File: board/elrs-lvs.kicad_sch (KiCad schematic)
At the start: 150 parts, among them J1 PWM, J10 CF/Prog, J11 Holes, J12 Balance, J13 U.FL, J2 PWM, J3 PWM, J4 PWM, J5 PWM, J6 PWM, J7 PWM, J8 PWM, J9 Little Tower, SW1 SW_SPST, SW2 SW_SPST, U1 ESP32-PICO-V3, U2 SX1281, U3 TPSM82901SISR, U4 2450FM07D0034T, Y1 52Mhz TCXO

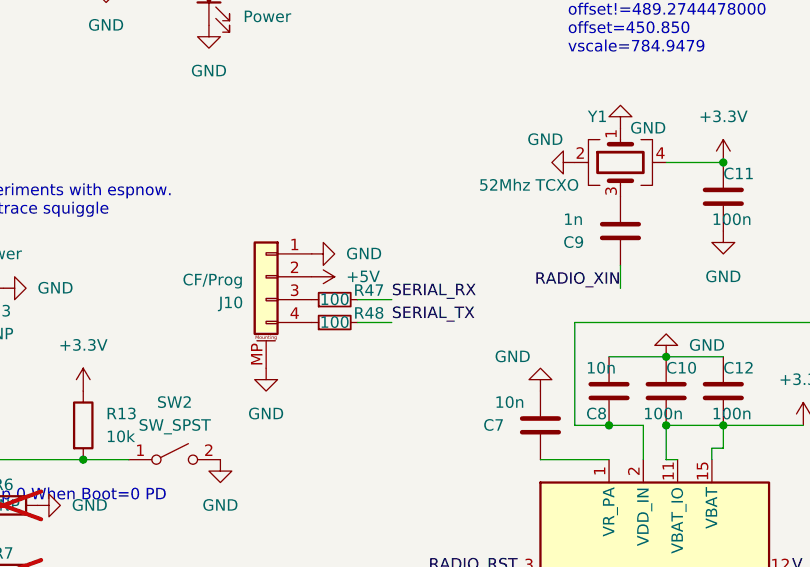
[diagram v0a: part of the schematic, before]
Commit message: invert serial connector pinout
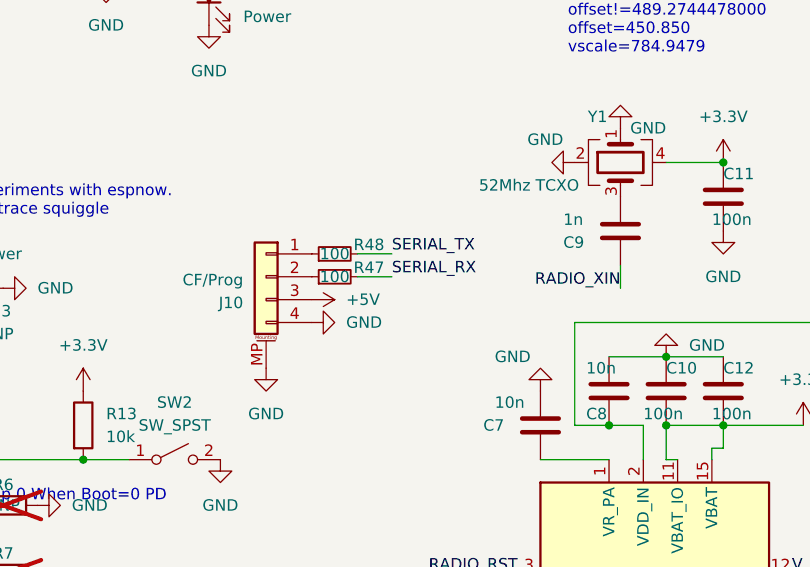
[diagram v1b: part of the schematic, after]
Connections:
- net +5V: now also J10.3 (Pin_3); no longer J10.2 (Pin_2)
- net GND: now also J10.4 (Pin_4); no longer J10.1 (Pin_1)
- net at R48.1: now also J10.1 (Pin_1); no longer J10.4 (Pin_4)
- net at R47.1: now also J10.2 (Pin_2); no longer J10.3 (Pin_3)
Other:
- moved on the sheet: R47, R48
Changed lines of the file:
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@@
 	(wire
 		(pts
-			(xy 157.48 72.39) (xy 161.29 72.39)
+			(xy 157.48 64.77) (xy 161.29 64.77)
 		)
 		(stroke
@@
 	(wire
 		(pts
-			(xy 157.48 69.85) (xy 161.29 69.85)
+			(xy 157.48 67.31) (xy 161.29 67.31)
 		)
 		(stroke
@@
 	)
 	(label "SERIAL_TX"
-		(at 161.29 72.39 0)
+		(at 161.29 64.77 0)
 		(effects
 			(font
@@
 	)
 	(label "SERIAL_RX"
-		(at 161.29 69.85 0)
+		(at 161.29 67.31 0)
 		(effects
 			(font
@@
 	(symbol
 		(lib_id "Device:R_Small")
-		(at 154.94 72.39 90)
+		(at 154.94 64.77 90)
 		(unit 1)
 		(exclude_from_sim no)
@@
 		(dnp no)
 		(property "Reference" "R48"
-			(at 158.75 71.374 90)
+			(at 158.75 63.754 90)
 			(effects
 				(font
@@
 		)
 		(property "Value" "100"
-			(at 154.94 72.39 90)
+			(at 154.94 64.77 90)
 			(effects
 				(font
@@
 		)
 		(property "Footprint" "Resistor_SMD:R_0402_1005Metric"
-			(at 154.94 72.39 0)
+			(at 154.94 64.77 0)
 			(effects
 				(font
@@
 		)
 		(property "Datasheet" "~"
-			(at 154.94 72.39 0)
+			(at 154.94 64.77 0)
 			(effects
 				(font
@@
 		)
 		(property "Description" "Resistor, small symbol"
-			(at 154.94 72.39 0)
+			(at 154.94 64.77 0)
 			(effects
 				(font
@@
 		)
 		(property "Digikey" "https://www.digikey.com/en/products/detail/yageo/AC0402JR-07100RL/5895570"
-			(at 154.94 72.39 0)
+			(at 154.94 64.77 0)
 			(effects
 				(font
@@
 		)
 		(property "Manufacturer" "Yageo"
-			(at 154.94 72.39 0)
+			(at 154.94 64.77 0)
 			(effects
 				(font
@@
 		)
 		(property "Part" "AC0402JR-07100RL"
-			(at 154.94 72.39 0)
+			(at 154.94 64.77 0)
 			(effects
 				(font
@@
 	(symbol
 		(lib_id "Device:R_Small")
-		(at 154.94 69.85 90)
+		(at 154.94 67.31 90)
 		(unit 1)
 		(exclude_from_sim no)
@@
 		(dnp no)
 		(property "Reference" "R47"
-			(at 158.75 68.834 90)
+			(at 158.75 66.294 90)
 			(effects
 				(font
@@
 		)
 		(property "Value" "100"
-			(at 154.94 69.85 90)
+			(at 154.94 67.31 90)
 			(effects
 				(font
@@
 		)
 		(property "Footprint" "Resistor_SMD:R_0402_1005Metric"
-			(at 154.94 69.85 0)
+			(at 154.94 67.31 0)
 			(effects
 				(font
@@
 		)
 		(property "Datasheet" "~"
-			(at 154.94 69.85 0)
+			(at 154.94 67.31 0)
 			(effects
 				(font
@@
 		)
 		(property "Description" "Resistor, small symbol"
-			(at 154.94 69.85 0)
+			(at 154.94 67.31 0)
 			(effects
 				(font
@@
 		)
 		(property "Digikey" "https://www.digikey.com/en/products/detail/yageo/AC0402JR-07100RL/5895570"
-			(at 154.94 69.85 0)
+			(at 154.94 67.31 0)
 			(effects
 				(font
@@
 		)
 		(property "Manufacturer" "Yageo"
-			(at 154.94 69.85 0)
+			(at 154.94 67.31 0)
 			(effects
 				(font
@@
 		)
 		(property "Part" "AC0402JR-07100RL"
-			(at 154.94 69.85 0)
+			(at 154.94 67.31 0)
 			(effects
 				(font
@@
 	(symbol
 		(lib_id "power:+5V")
-		(at 152.4 67.31 270)
+		(at 152.4 69.85 270)
 		(unit 1)
 		(exclude_from_sim no)
@@
 		(fields_autoplaced yes)
 		(property "Reference" "#PWR051"
-			(at 148.59 67.31 0)
+			(at 148.59 69.85 0)
 			(effects
 				(font
@@
 		)
 		(property "Value" "+5V"
-			(at 156.21 67.3099 90)
+			(at 156.21 69.8499 90)
 			(effects
 				(font
@@
 		)
 		(property "Footprint" ""
-			(at 152.4 67.31 0)
+			(at 152.4 69.85 0)
 			(effects
 				(font
@@
 		)
 		(property "Datasheet" ""
-			(at 152.4 67.31 0)
+			(at 152.4 69.85 0)
 			(effects
 				(font
@@
 		)
 		(property "Description" "Power symbol creates a global label with name \"+5V\""
-			(at 152.4 67.31 0)
+			(at 152.4 69.85 0)
 			(effects
 				(font
@@
 	(symbol
 		(lib_id "power:GND")
-		(at 152.4 64.77 90)
+		(at 152.4 72.39 90)
 		(unit 1)
 		(exclude_from_sim no)
@@
 		(fields_autoplaced yes)
 		(property "Reference" "#PWR050"
-			(at 158.75 64.77 0)
+			(at 158.75 72.39 0)
 			(effects
 				(font
@@
 		)
 		(property "Value" "GND"
-			(at 156.21 64.7699 90)
+			(at 156.21 72.3899 90)
 			(effects
 				(font
@@
 		)
 		(property "Footprint" ""
-			(at 152.4 64.77 0)
+			(at 152.4 72.39 0)
 			(effects
 				(font
@@
 		)
 		(property "Datasheet" ""
-			(at 152.4 64.77 0)
+			(at 152.4 72.39 0)
 			(effects
 				(font
@@
 		)
 		(property "Description" "Power symbol creates a global label with name \"GND\" , ground"
-			(at 152.4 64.77 0)
+			(at 152.4 72.39 0)
 			(effects
 				(font

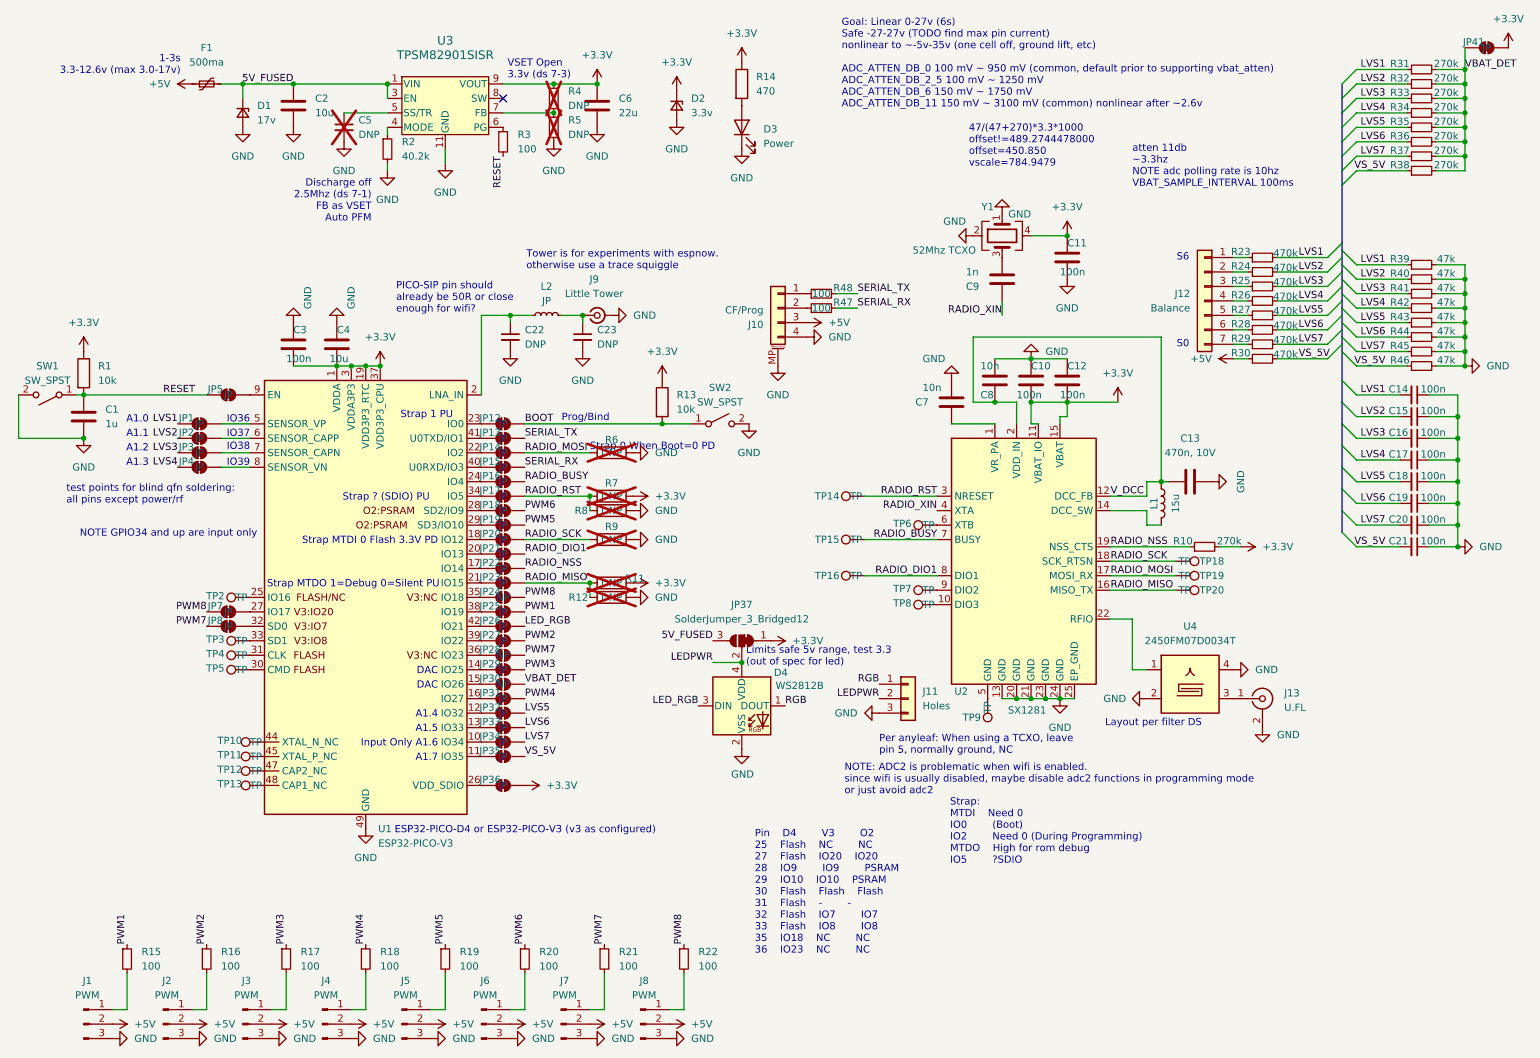
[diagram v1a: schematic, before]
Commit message: remove dnp options and test points
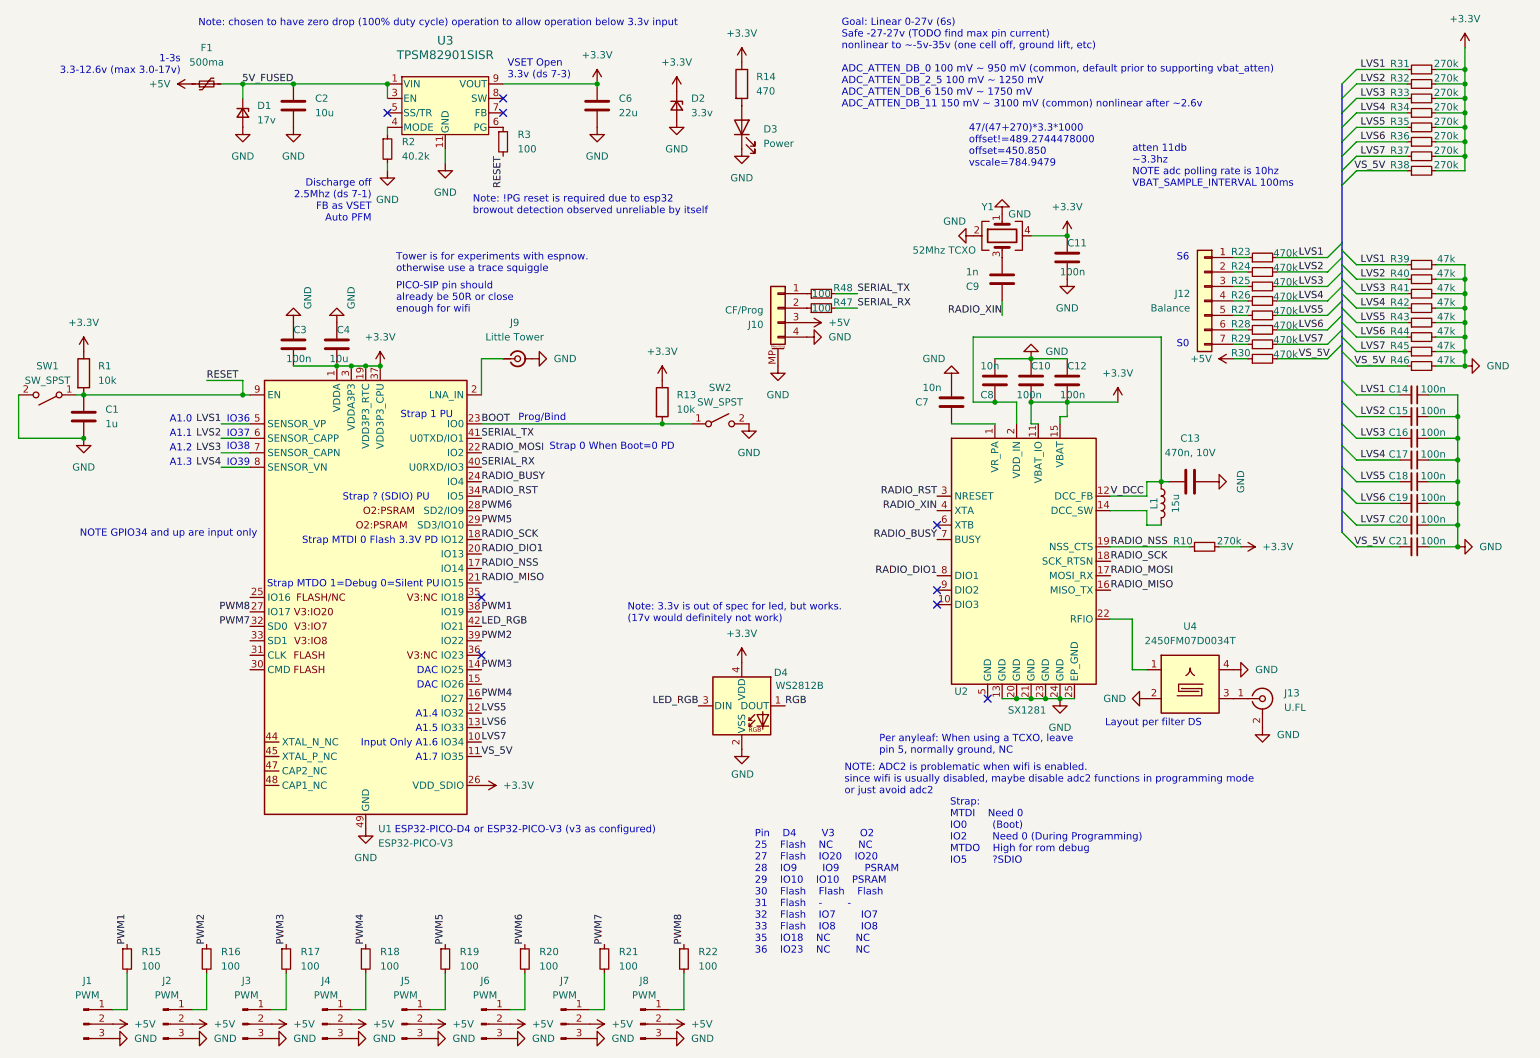
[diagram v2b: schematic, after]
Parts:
- removed C22, C23: DNP, elrs-lvs:R_0201_0603_NP, symbol Device:C_Small
- removed C5: DNP, Capacitor_SMD:C_0402_1005Metric, symbol Device:C_Small
- removed J11: Holes, Connector_PinHeader_2.54mm:PinHeader_1x03_P2.54mm_Vertical, symbol Connector_Generic:Conn_01x03
- removed JP1, JP12, JP13, JP14, JP15, JP16, JP17, JP18, JP19, JP2, JP20, JP21, JP22, JP23, JP25, JP26, JP27, JP29, JP3, JP31, JP32, JP33, JP34, JP35, JP36, JP4, JP41, JP5, JP7, JP8: JP, elrs-lvs:R_0201_0603_JP, symbol Jumper:SolderJumper_2_Bridged
- removed JP24, JP28, JP30: NP, elrs-lvs:R_0201_0603_NP, symbol Jumper:SolderJumper_2_Open
- removed JP37: SolderJumper_3_Bridged12, elrs-lvs:R_0201_0603_JP_123, symbol Jumper:SolderJumper_3_Bridged12
- removed L2: JP, elrs-lvs:R_0201_0603_JP, symbol Device:L_Small
- removed R11, R12, R6, R7, R8, R9: DNP, Resistor_SMD:R_0402_1005Metric, symbol Device:R
- removed R4, R5: DNP, Resistor_SMD:R_0402_1005Metric, symbol Device:R_Small
- removed TP10, TP11, TP12, TP13, TP14, TP15, TP16, TP18, TP19, TP2, TP20, TP3, TP4, TP5, TP6, TP7, TP8, TP9: TP, elrs-lvs:TestPoint_Pad_D0.25mm, symbol Connector:TestPoint
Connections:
- net LEDPWR is gone; now on net +3.3V: D4.4 (VDD)
- net VBAT_DET is gone; now on net +3.3V: R31.2, R32.2, R33.2, R34.2, R35.2, R36.2, R37.2, R38.2
- net +3.3V: now also U1.26 (VDD_SDIO)
- net BOOT: now also U1.23 (IO0)
- net LED_RGB: now also U1.42 (IO21)
- net LVS1: now also U1.5 (SENSOR_VP)
- net LVS2: now also U1.6 (SENSOR_CAPP)
- net LVS3: now also U1.7 (SENSOR_CAPN)
- net LVS4: now also U1.8 (SENSOR_VN)
- net LVS5: now also U1.12 (IO32)
- net LVS6: now also U1.13 (IO33)
- net LVS7: now also U1.10 (IO34)
- net PWM1: now also U1.38 (IO19)
- net PWM2: now also U1.39 (IO22)
- net PWM3: now also U1.14 (IO25)
- net PWM4: now also U1.16 (IO27)
- net PWM5: now also U1.29 (SD3/IO10)
- net PWM6: now also U1.28 (SD2/IO9)
- net PWM7: now also U1.32 (SD0)
- net PWM8: now also U1.27 (IO17)
- net RADIO_BUSY: now also U1.24 (IO4)
- net RADIO_DIO1: now also U1.20 (IO13)
- net RADIO_MISO: now also U1.21 (IO15)
- net RADIO_MOSI: now also U1.22 (IO2)
- net RADIO_NSS: now also U1.17 (IO14)
- net RADIO_RST: now also U1.34 (IO5)
- net RADIO_SCK: now also U1.18 (IO12)
- net RESET: now also U1.9 (EN)
- net SERIAL_RX: now also U1.40 (U0RXD/IO3)
- net SERIAL_TX: now also U1.41 (U0TXD/IO1)
- net VS_5V: now also U1.11 (IO35)
- net at U1.2 (LNA_IN): now also J9.1 (In)
- no-connect marks 1 -> 9
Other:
- note added: "Note: !PG reset is required due to esp32 browout detection observed unreliable by itself"
- note added: "Note: 3.3v is out of spec for led, but works. (17v would definitely not work)"
- note added: "Note: chosen to have zero drop (100% duty cycle) operation to allow operation below 3.3v input"
- note added: "PICO-SIP pin should already be 50R or close enough for wifi"
- note removed: "Limits safe 5v range, test 3.3 (out of spec for led)"
- note removed: "PICO-SIP pin should already be 50R or close enough for wifi?"
- note removed: "test points for blind qfn soldering: all pins except power/rf"
- moved on the sheet: J9

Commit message: initial placement for single sided lower density
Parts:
- J12: footprint Connector_JST:JST_XH_S7B-XH-A-1_1x07_P2.50mm_Horizontal -> elrs-lvs:JST_XH_S7B-XH-A-1_1x07_P2.50mm_Horizontal_Zero_Clearance
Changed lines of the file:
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@@
 			)
 		)
-		(property "Footprint" "Connector_JST:JST_XH_S7B-XH-A-1_1x07_P2.50mm_Horizontal"
+		(property "Footprint" "elrs-lvs:JST_XH_S7B-XH-A-1_1x07_P2.50mm_Horizontal_Zero_Clearance"
 			(at 222.25 66.04 0)
 			(effects

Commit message: export for review
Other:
- note added: "V2: invert serial connector pinout (to match radiomaster), remove test points, re-layout for single sided and larger (cheaper) clearances"
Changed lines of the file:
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@@
+		)
+	)
+	(text "V2: invert serial connector pinout (to match radiomaster),\nremove test points, re-layout for single sided and larger (cheaper) clearances"
+		(exclude_from_sim no)
+		(at 177.8 166.878 0)
+		(effects
+			(font
+				(size 1.27 1.27)
+			)
+			(justify left top)
 		)
 	)

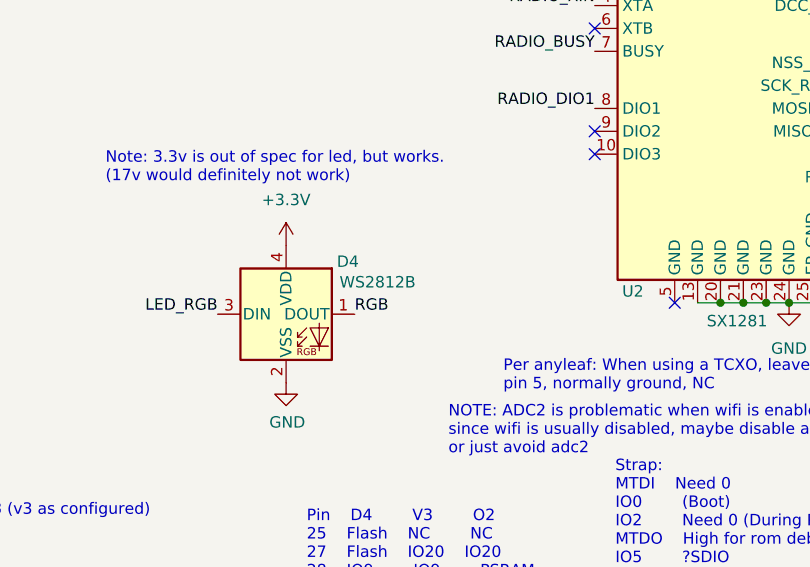
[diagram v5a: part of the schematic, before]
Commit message: change D2 to unidirectional, add most lcsc numbers (alternates needed for some parts)
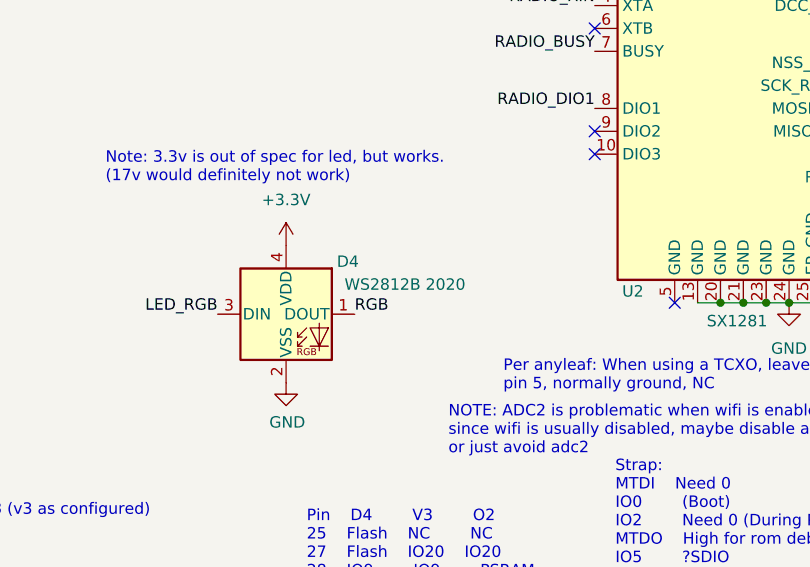
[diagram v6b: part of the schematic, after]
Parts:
- C1: LCSC (none) -> C318573
- C10, C11, C12, C14, C15, C16, C17, C18, C19, C20, C21, C3: LCSC C1525 -> C100072
- C2: LCSC (none) -> C5646740
- C6: LCSC (none) -> C2167548
- C9: LCSC C1523 -> C2168479
- D1: LCSC (none) -> C7236804
- D2: Digikey https://www.digikey.com/en/products/detail/panjit-international-inc/PJGBLC03C-AU-R1-000A1/15797697 -> https://www.digikey.com/en/products/detail/panjit-international-inc/PJGBLC03-AU-R1-000A1/15798010?s=N4IgTCBcDaIAoCkDiAhAMgYQAwGYC0AggKogC6AvkA; LCSC (none) -> C6951951; Part PJGBLC03C-AU_R1_000A1 -> PJGBLC03-AU_R1_000A1
- D3: LCSC (none) -> C20562575
- D4: value WS2812B -> WS2812B 2020; Digikey 1528-4684-ND -> 1528-4684-ND (Adafruit 4684); Manufacturer Adafruit -> Multiple; Part 4684 -> WS2812B-2020
- F1: LCSC (none) -> C634245
- J12: LCSC (none) -> C491713
- J9: Digikey (none) -> https://www.digikey.com/en/products/detail/molex/0479480001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; LCSC (none) -> C152351
- L1: Digikey (none) -> https://www.digikey.com/en/products/detail/tdk/MLZ2012M150W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
- R1, R13: LCSC (none) -> C144731
- R10, R31, R32, R33, R34, R35, R36, R37, R38: LCSC (none) -> C163475
- R14: LCSC (none) -> C144711
- R15, R16, R17, R18, R19, R20, R21, R22, R3, R47, R48: LCSC (none) -> C138288
- R2: LCSC (none) -> C144760
- R23, R24, R25, R26, R27, R28, R29, R30: LCSC (none) -> C4001349
- R39, R40, R41, R42, R43, R44, R45, R46: LCSC (none) -> C93943
- SW1, SW2: LCSC (none) -> C4364937
- U1: Digikey (none) -> https://www.digikey.com/en/products/detail/espressif-system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; LCSC (none) -> C967022
- U2: LCSC C125969 -> C2151551
- U3: LCSC (none) -> C6290581
- U4: LCSC (none) -> C2651081
- Y1: LCSC (none) -> C22434896
